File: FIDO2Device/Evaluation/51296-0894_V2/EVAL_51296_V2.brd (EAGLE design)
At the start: 25 x 38 mm, 25 parts, among them CN1 51296-0894, CN2 IF_6PIN, CN3 IF_3PIN, CN4 IF_4PIN, Q1 BSS84AKQBZ, U1 RV-3028-C7

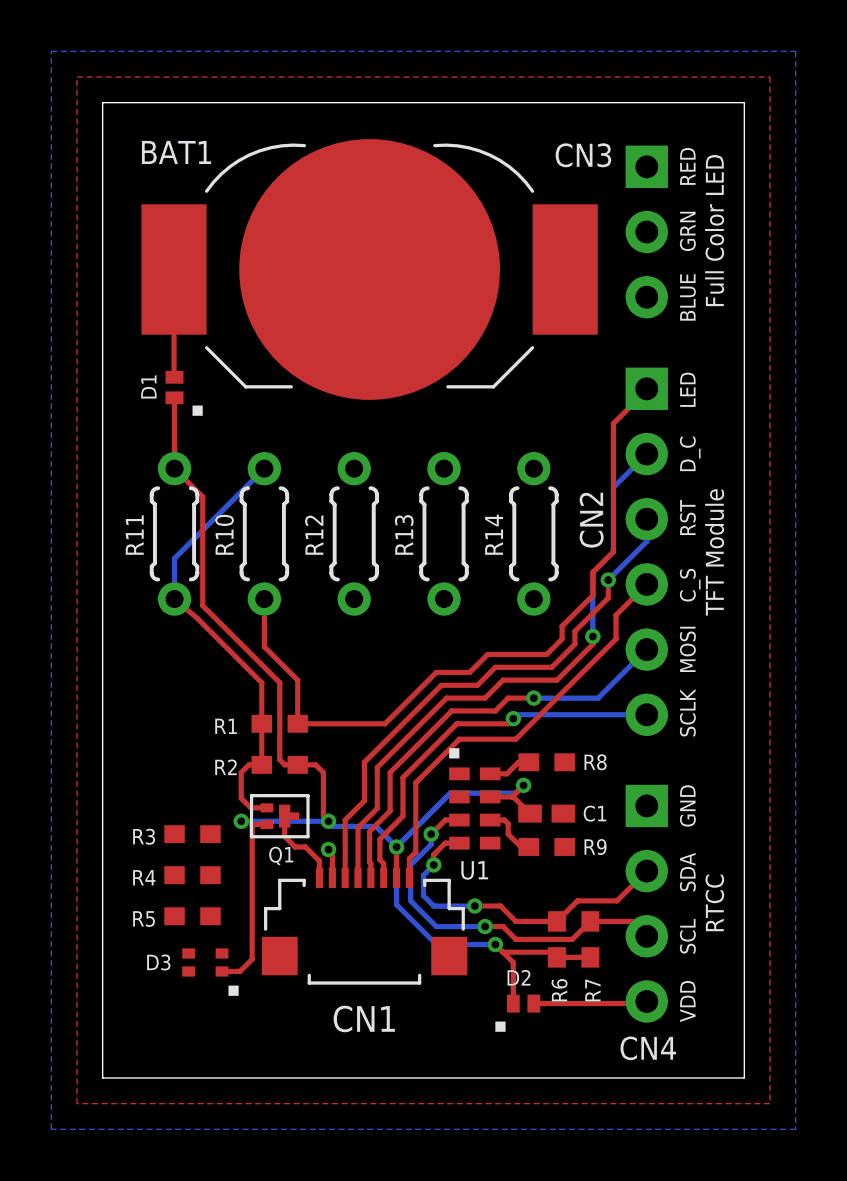
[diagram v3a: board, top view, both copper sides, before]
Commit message: レイアウトを修正
・LED_Bの配線
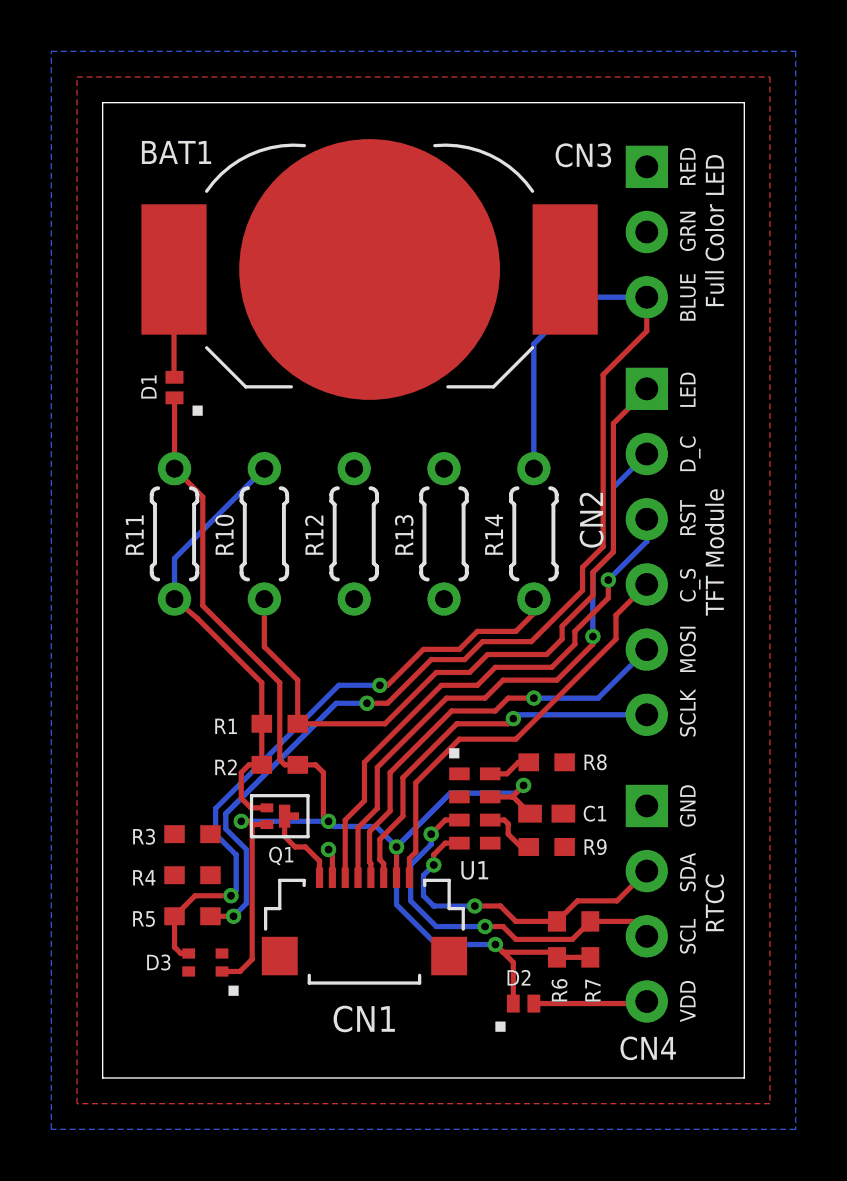
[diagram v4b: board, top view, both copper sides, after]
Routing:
- net LED_B: track 0.00 -> 45.4 mm, vias 0 -> 2
- net N$10: track 0.00 -> 24.3 mm, vias 0 -> 2
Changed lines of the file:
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@@
 <contactref element="R5" pad="1"/>
 <contactref element="R14" pad="1"/>
-<wire x1="16.8" y1="23.74" x2="21.2" y2="30.42" width="0" layer="19" extent="1-1"/>
-<wire x1="4.2" y1="6.3" x2="16.8" y2="23.74" width="0" layer="19" extent="1-1"/>
+<via x="5.1" y="6.3" extent="1-16" drill="0.3"/>
+<wire x1="5.1" y1="6.3" x2="5.6" y2="6.8" width="0.2032" layer="16"/>
+<wire x1="5.6" y1="6.8" x2="5.6" y2="8.9" width="0.2032" layer="16"/>
+<wire x1="5.6" y1="8.9" x2="4.8" y2="9.7" width="0.2032" layer="16"/>
+<wire x1="4.8" y1="9.7" x2="4.8" y2="10.3" width="0.2032" layer="16"/>
+<wire x1="4.8" y1="10.3" x2="9.1" y2="14.6" width="0.2032" layer="16"/>
+<wire x1="9.1" y1="14.6" x2="10.3" y2="14.6" width="0.2032" layer="16"/>
+<via x="10.3" y="14.6" extent="1-16" drill="0.3"/>
+<wire x1="10.3" y1="14.6" x2="11.1" y2="14.6" width="0.2032" layer="1"/>
+<wire x1="11.1" y1="14.6" x2="12.8" y2="16.3" width="0.2032" layer="1"/>
+<wire x1="12.8" y1="16.3" x2="14.1" y2="16.3" width="0.2032" layer="1"/>
+<wire x1="14.1" y1="16.3" x2="14.8" y2="17" width="0.2032" layer="1"/>
+<wire x1="16.7" y1="17" x2="18.7" y2="19" width="0.2032" layer="1"/>
+<wire x1="18.7" y1="19" x2="18.7" y2="19.9" width="0.2032" layer="1"/>
+<wire x1="18.7" y1="19.9" x2="19.5" y2="20.7" width="0.2032" layer="1"/>
+<wire x1="19.5" y1="20.7" x2="19.5" y2="27.4" width="0.2032" layer="1"/>
+<wire x1="19.5" y1="27.4" x2="21.2" y2="29.1" width="0.2032" layer="1"/>
+<wire x1="21.2" y1="30.42" x2="21.2" y2="29.1" width="0.2032" layer="1"/>
+<wire x1="4.2" y1="6.3" x2="5.1" y2="6.3" width="0.2032" layer="1"/>
+<wire x1="14.8" y1="17" x2="16.7" y2="17" width="0.2032" layer="1"/>
+<wire x1="21.2" y1="30.42" x2="18.62" y2="30.42" width="0.2032" layer="16"/>
+<wire x1="18.62" y1="30.42" x2="16.8" y2="28.6" width="0.2032" layer="16"/>
+<wire x1="16.8" y1="23.74" x2="16.8" y2="28.6" width="0.2032" layer="16"/>
 </signal>
 <signal name="N$6">
@@
 <contactref element="R5" pad="2"/>
 <contactref element="R14" pad="2"/>
-<wire x1="2.8" y1="6.3" x2="16.8" y2="18.66" width="0" layer="19" extent="1-1"/>
-<wire x1="3.35" y1="4.85" x2="2.8" y2="6.3" width="0" layer="19" extent="1-1"/>
+<via x="5" y="7.1" extent="1-16" drill="0.3"/>
+<wire x1="5" y1="7.1" x2="3.6" y2="7.1" width="0.2032" layer="1"/>
+<wire x1="3.6" y1="7.1" x2="2.8" y2="6.3" width="0.2032" layer="1"/>
+<wire x1="5" y1="7.1" x2="5.2" y2="7.3" width="0.2032" layer="16"/>
+<wire x1="5.2" y1="7.3" x2="5.2" y2="8.7" width="0.2032" layer="16"/>
+<wire x1="5.2" y1="8.7" x2="4.4" y2="9.5" width="0.2032" layer="16"/>
+<wire x1="4.4" y1="9.5" x2="4.4" y2="10.5" width="0.2032" layer="16"/>
+<wire x1="4.4" y1="10.5" x2="9.2" y2="15.3" width="0.2032" layer="16"/>
+<wire x1="9.2" y1="15.3" x2="10.8" y2="15.3" width="0.2032" layer="16"/>
+<via x="10.8" y="15.3" extent="1-16" drill="0.3"/>
+<wire x1="10.8" y1="15.3" x2="11.1" y2="15.3" width="0.2032" layer="1"/>
+<wire x1="11.1" y1="15.3" x2="12.5" y2="16.7" width="0.2032" layer="1"/>
+<wire x1="12.5" y1="16.7" x2="13.9" y2="16.7" width="0.2032" layer="1"/>
+<wire x1="13.9" y1="16.7" x2="14.6" y2="17.4" width="0.2032" layer="1"/>
+<wire x1="14.6" y1="17.4" x2="16.1" y2="17.4" width="0.2032" layer="1"/>
+<wire x1="16.8" y1="18.66" x2="16.8" y2="18.1" width="0.2032" layer="1"/>
+<wire x1="16.8" y1="18.1" x2="16.1" y2="17.4" width="0.2032" layer="1"/>
+<wire x1="2.8" y1="6.3" x2="2.8" y2="5.1" width="0.2032" layer="1"/>
+<wire x1="3.05" y1="4.85" x2="2.8" y2="5.1" width="0.2032" layer="1"/>
+<wire x1="3.05" y1="4.85" x2="3.35" y2="4.85" width="0.2032" layer="1"/>
 </signal>
 </signals>

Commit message: レイアウトを修正
・LED_Gの配線
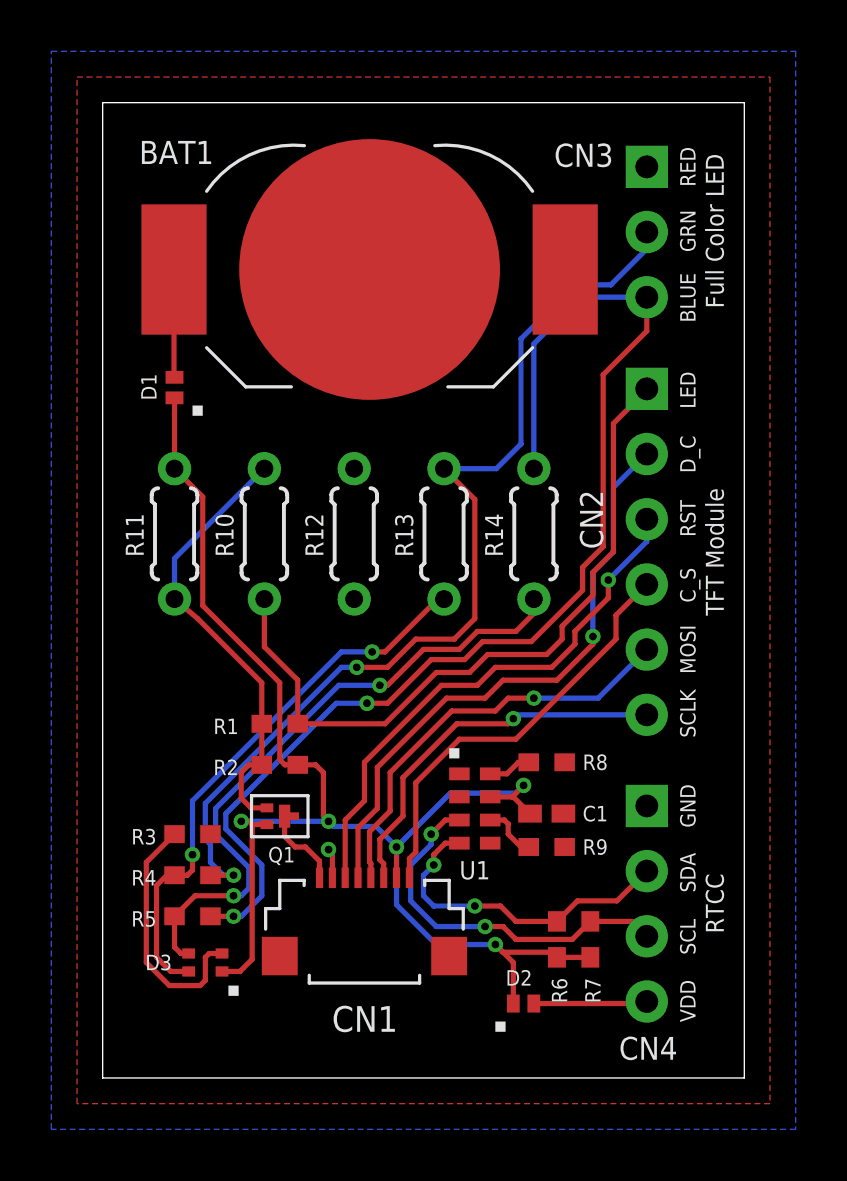
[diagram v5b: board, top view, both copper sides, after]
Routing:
- net LED_G: track 0.00 -> 38.7 mm, vias 0 -> 2
- net N$9: track 0.00 -> 21.7 mm, vias 0 -> 2
- net N$6: track 0.00 -> 9.82 mm
- net LED_B: track 45.4 -> 46.1 mm
- net N$10: track 24.3 -> 25.0 mm
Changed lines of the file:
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@@
 <contactref element="R4" pad="1"/>
 <contactref element="R13" pad="1"/>
-<wire x1="13.3" y1="23.74" x2="21.2" y2="32.96" width="0" layer="19" extent="1-1"/>
-<wire x1="4.2" y1="7.9" x2="13.3" y2="23.74" width="0" layer="19" extent="1-1"/>
+<wire x1="21.2" y1="32.96" x2="21.2" y2="32.3" width="0.2032" layer="16"/>
+<wire x1="21.2" y1="32.3" x2="19.8" y2="30.9" width="0.2032" layer="16"/>
+<wire x1="19.8" y1="30.9" x2="18.4" y2="30.9" width="0.2032" layer="16"/>
+<wire x1="18.4" y1="30.9" x2="16.3" y2="28.8" width="0.2032" layer="16"/>
+<wire x1="16.3" y1="28.8" x2="16.3" y2="24.7" width="0.2032" layer="16"/>
+<wire x1="16.3" y1="24.7" x2="15.34" y2="23.74" width="0.2032" layer="16"/>
+<wire x1="13.3" y1="23.74" x2="15.34" y2="23.74" width="0.2032" layer="16"/>
+<via x="5.1" y="7.9" extent="1-16" drill="0.3"/>
+<wire x1="4.2" y1="7.9" x2="5.1" y2="7.9" width="0.2032" layer="1"/>
+<wire x1="4" y1="9.3" x2="4" y2="10.7" width="0.2032" layer="16"/>
+<wire x1="4" y1="9.3" x2="4.2" y2="9.1" width="0.2032" layer="16"/>
+<wire x1="4.2" y1="9.1" x2="4.2" y2="8.4" width="0.2032" layer="16"/>
+<wire x1="4.2" y1="8.4" x2="4.7" y2="7.9" width="0.2032" layer="16"/>
+<wire x1="4.7" y1="7.9" x2="5.1" y2="7.9" width="0.2032" layer="16"/>
+<wire x1="4" y1="10.7" x2="9.3" y2="16" width="0.2032" layer="16"/>
+<wire x1="9.3" y1="16" x2="9.9" y2="16" width="0.2032" layer="16"/>
+<via x="9.9" y="16" extent="1-16" drill="0.3"/>
+<wire x1="9.9" y1="16" x2="11.1" y2="16" width="0.2032" layer="1"/>
+<wire x1="11.1" y1="16" x2="12.2" y2="17.1" width="0.2032" layer="1"/>
+<wire x1="12.2" y1="17.1" x2="13.7" y2="17.1" width="0.2032" layer="1"/>
+<wire x1="13.7" y1="17.1" x2="14.5" y2="17.9" width="0.2032" layer="1"/>
+<wire x1="14.5" y1="17.9" x2="14.5" y2="22.54" width="0.2032" layer="1"/>
+<wire x1="14.5" y1="22.54" x2="13.3" y2="23.74" width="0.2032" layer="1"/>
 </signal>
 <signal name="LED_B">
@@
 <contactref element="R14" pad="1"/>
 <via x="5.1" y="6.3" extent="1-16" drill="0.3"/>
-<wire x1="5.1" y1="6.3" x2="5.6" y2="6.8" width="0.2032" layer="16"/>
-<wire x1="5.6" y1="6.8" x2="5.6" y2="8.9" width="0.2032" layer="16"/>
-<wire x1="5.6" y1="8.9" x2="4.8" y2="9.7" width="0.2032" layer="16"/>
 <wire x1="4.8" y1="9.7" x2="4.8" y2="10.3" width="0.2032" layer="16"/>
 <wire x1="4.8" y1="10.3" x2="9.1" y2="14.6" width="0.2032" layer="16"/>
@@
 <wire x1="18.62" y1="30.42" x2="16.8" y2="28.6" width="0.2032" layer="16"/>
 <wire x1="16.8" y1="23.74" x2="16.8" y2="28.6" width="0.2032" layer="16"/>
+<wire x1="5.1" y1="6.3" x2="5.4" y2="6.3" width="0.2032" layer="16"/>
+<wire x1="5.4" y1="6.3" x2="6.2" y2="7.1" width="0.2032" layer="16"/>
+<wire x1="6.2" y1="7.1" x2="6.2" y2="8.3" width="0.2032" layer="16"/>
+<wire x1="6.2" y1="8.3" x2="4.8" y2="9.7" width="0.2032" layer="16"/>
 </signal>
 <signal name="N$6">
@@
 <contactref element="R3" pad="2"/>
 <contactref element="R12" pad="2"/>
+<wire x1="4.65" y1="4.85" x2="4.15" y2="4.85" width="0.2032" layer="1"/>
+<wire x1="4.15" y1="4.85" x2="4" y2="4.7" width="0.2032" layer="1"/>
+<wire x1="4" y1="4.7" x2="4" y2="3.8" width="0.2032" layer="1"/>
+<wire x1="4" y1="3.8" x2="3.8" y2="3.6" width="0.2032" layer="1"/>
+<wire x1="3.8" y1="3.6" x2="2.6" y2="3.6" width="0.2032" layer="1"/>
+<wire x1="2.6" y1="3.6" x2="1.7" y2="4.5" width="0.2032" layer="1"/>
+<wire x1="1.7" y1="4.5" x2="1.7" y2="8.4" width="0.2032" layer="1"/>
+<wire x1="1.7" y1="8.4" x2="2.8" y2="9.5" width="0.2032" layer="1"/>
 <wire x1="2.8" y1="9.5" x2="9.8" y2="18.66" width="0" layer="19" extent="1-1"/>
-<wire x1="4.65" y1="4.85" x2="2.8" y2="9.5" width="0" layer="19" extent="1-1"/>
 </signal>
 <signal name="N$9">
@@
 <contactref element="R13" pad="2"/>
 <contactref element="D3" pad="4"/>
-<wire x1="2.8" y1="7.9" x2="13.3" y2="18.66" width="0" layer="19" extent="1-1"/>
-<wire x1="3.35" y1="4.15" x2="2.8" y2="7.9" width="0" layer="19" extent="1-1"/>
+<wire x1="3.35" y1="4.15" x2="2.65" y2="4.15" width="0.2032" layer="1"/>
+<wire x1="2.65" y1="4.15" x2="2.1" y2="4.7" width="0.2032" layer="1"/>
+<wire x1="2.1" y1="4.7" x2="2.1" y2="7.5" width="0.2032" layer="1"/>
+<wire x1="2.8" y1="7.9" x2="2.5" y2="7.9" width="0.2032" layer="1"/>
+<wire x1="2.5" y1="7.9" x2="2.1" y2="7.5" width="0.2032" layer="1"/>
+<via x="3.5" y="8.7" extent="1-16" drill="0.3"/>
+<wire x1="2.8" y1="7.9" x2="3.3" y2="7.9" width="0.2032" layer="1"/>
+<wire x1="3.3" y1="7.9" x2="3.5" y2="8.1" width="0.2032" layer="1"/>
+<wire x1="3.5" y1="8.1" x2="3.5" y2="8.7" width="0.2032" layer="1"/>
+<wire x1="3.5" y1="8.7" x2="3.5" y2="10.8" width="0.2032" layer="16"/>
+<wire x1="3.5" y1="10.8" x2="9.3" y2="16.6" width="0.2032" layer="16"/>
+<wire x1="9.3" y1="16.6" x2="10.5" y2="16.6" width="0.2032" layer="16"/>
+<via x="10.5" y="16.6" extent="1-16" drill="0.3"/>
+<wire x1="10.5" y1="16.6" x2="11" y2="16.6" width="0.2032" layer="1"/>
+<wire x1="13.3" y1="18.66" x2="13.06" y2="18.66" width="0.2032" layer="1"/>
+<wire x1="13.06" y1="18.66" x2="11" y2="16.6" width="0.2032" layer="1"/>
 </signal>
 <signal name="N$10">
@@
 <contactref element="R5" pad="2"/>
 <contactref element="R14" pad="2"/>
-<via x="5" y="7.1" extent="1-16" drill="0.3"/>
-<wire x1="5" y1="7.1" x2="3.6" y2="7.1" width="0.2032" layer="1"/>
+<via x="5.1" y="7.1" extent="1-16" drill="0.3"/>
+<wire x1="5.1" y1="7.1" x2="3.6" y2="7.1" width="0.2032" layer="1"/>
 <wire x1="3.6" y1="7.1" x2="2.8" y2="6.3" width="0.2032" layer="1"/>
-<wire x1="5" y1="7.1" x2="5.2" y2="7.3" width="0.2032" layer="16"/>
-<wire x1="5.2" y1="7.3" x2="5.2" y2="8.7" width="0.2032" layer="16"/>
-<wire x1="5.2" y1="8.7" x2="4.4" y2="9.5" width="0.2032" layer="16"/>
 <wire x1="4.4" y1="9.5" x2="4.4" y2="10.5" width="0.2032" layer="16"/>
 <wire x1="4.4" y1="10.5" x2="9.2" y2="15.3" width="0.2032" layer="16"/>
@@
 <wire x1="3.05" y1="4.85" x2="2.8" y2="5.1" width="0.2032" layer="1"/>
 <wire x1="3.05" y1="4.85" x2="3.35" y2="4.85" width="0.2032" layer="1"/>
+<wire x1="5.1" y1="7.1" x2="5.4" y2="7.1" width="0.2032" layer="16"/>
+<wire x1="5.4" y1="7.1" x2="5.7" y2="7.4" width="0.2032" layer="16"/>
+<wire x1="5.7" y1="7.4" x2="5.7" y2="8.2" width="0.2032" layer="16"/>
+<wire x1="4.4" y1="9.5" x2="5.7" y2="8.2" width="0.2032" layer="16"/>
 </signal>
 </signals>

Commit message: レイアウトを修正
・LED_Rの配線
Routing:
- net LED_R: track 0.00 -> 36.8 mm, vias 0 -> 1
- net N$6: track 9.82 -> 21.9 mm, vias 0 -> 1
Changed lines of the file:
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@@
 </element>
 <element name="R1" library="Parts" package="R0402N" value="5.1k" x="6.9" y="13.8" smashed="yes" rot="R180">
-<attribute name="NAME" x="5.3" y="14" size="0.6" layer="25" rot="R180"/>
+<attribute name="NAME" x="8.3" y="13.5" size="0.6" layer="25"/>
 <attribute name="VALUE" x="7.4" y="15.1" size="0.6" layer="27" rot="R180"/>
 </element>
 <element name="R2" library="Parts" package="R0402N" value="20k" x="6.9" y="12.2" smashed="yes">
-<attribute name="NAME" x="5.3" y="12.4" size="0.6" layer="25" rot="R180"/>
+<attribute name="NAME" x="8.3" y="11.9" size="0.6" layer="25"/>
 <attribute name="VALUE" x="6.4" y="10.9" size="0.6" layer="27"/>
 </element>
@@
 <contactref element="R3" pad="1"/>
 <contactref element="R12" pad="1"/>
-<wire x1="9.8" y1="23.74" x2="21.2" y2="35.5" width="0" layer="19" extent="1-1"/>
-<wire x1="4.2" y1="9.5" x2="9.8" y2="23.74" width="0" layer="19" extent="1-1"/>
+<wire x1="9.8" y1="23.74" x2="11.74" y2="23.74" width="0.2032" layer="16"/>
+<wire x1="11.74" y1="23.74" x2="12.8" y2="24.8" width="0.2032" layer="16"/>
+<wire x1="12.8" y1="24.8" x2="15.4" y2="24.8" width="0.2032" layer="16"/>
+<wire x1="15.4" y1="24.8" x2="15.8" y2="25.2" width="0.2032" layer="16"/>
+<wire x1="15.8" y1="25.2" x2="15.8" y2="29" width="0.2032" layer="16"/>
+<wire x1="15.8" y1="29" x2="18.1" y2="31.3" width="0.2032" layer="16"/>
+<wire x1="18.1" y1="31.3" x2="19.4" y2="31.3" width="0.2032" layer="16"/>
+<wire x1="19.4" y1="31.3" x2="20" y2="31.9" width="0.2032" layer="16"/>
+<wire x1="20" y1="31.9" x2="20" y2="34.3" width="0.2032" layer="16"/>
+<wire x1="20" y1="34.3" x2="21.2" y2="35.5" width="0.2032" layer="16"/>
+<via x="5.6" y="14.7" extent="1-16" drill="0.3"/>
+<wire x1="8.8" y1="17.8" x2="8.8" y2="18.3" width="0.2032" layer="16"/>
+<wire x1="8.8" y1="18.3" x2="8.8" y2="19.2" width="0.2032" layer="16"/>
+<wire x1="8.8" y1="19.2" x2="9.8" y2="20.2" width="0.2032" layer="16"/>
+<wire x1="9.8" y1="20.2" x2="9.8" y2="23.74" width="0.2032" layer="16"/>
+<wire x1="4.2" y1="9.5" x2="4.2" y2="11.4" width="0.2032" layer="1"/>
+<wire x1="4.2" y1="11.4" x2="5.4" y2="12.6" width="0.2032" layer="1"/>
+<wire x1="5.4" y1="12.6" x2="5.4" y2="14.5" width="0.2032" layer="1"/>
+<wire x1="5.4" y1="14.5" x2="5.6" y2="14.7" width="0.2032" layer="1"/>
+<wire x1="5.6" y1="14.7" x2="6.2" y2="14.7" width="0.2032" layer="16"/>
+<wire x1="6.2" y1="14.7" x2="8.8" y2="17.3" width="0.2032" layer="16"/>
+<wire x1="8.8" y1="17.3" x2="8.8" y2="17.8" width="0.2032" layer="16"/>
 </signal>
 <signal name="LED_G">
@@
 <wire x1="1.7" y1="4.5" x2="1.7" y2="8.4" width="0.2032" layer="1"/>
 <wire x1="1.7" y1="8.4" x2="2.8" y2="9.5" width="0.2032" layer="1"/>
-<wire x1="2.8" y1="9.5" x2="9.8" y2="18.66" width="0" layer="19" extent="1-1"/>
+<via x="2.8" y="10.5" extent="1-16" drill="0.3"/>
+<wire x1="9.8" y1="18.66" x2="9.8" y2="17.7" width="0.2032" layer="16"/>
+<wire x1="9.8" y1="17.7" x2="2.8" y2="10.7" width="0.2032" layer="16"/>
+<wire x1="2.8" y1="10.7" x2="2.8" y2="10.5" width="0.2032" layer="16"/>
+<wire x1="2.8" y1="9.5" x2="2.8" y2="10.5" width="0.2032" layer="1"/>
 </signal>
 <signal name="N$9">
